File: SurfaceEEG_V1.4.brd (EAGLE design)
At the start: 160 x 100 mm, 67 parts, among them IC1 LMV602, IC2 TSZ124IQ4T, U1 MCP4442-103E/ST

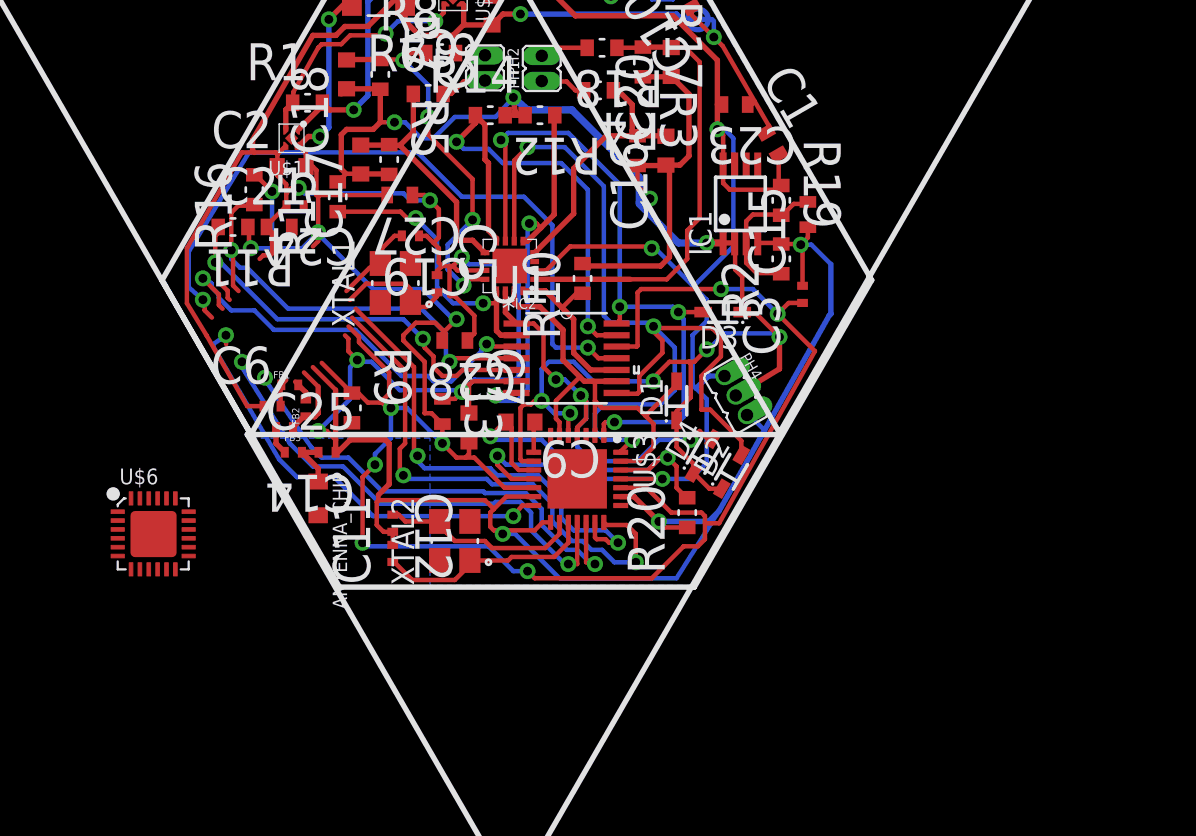
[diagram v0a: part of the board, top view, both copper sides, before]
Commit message: Started version 1.4 with atmega328
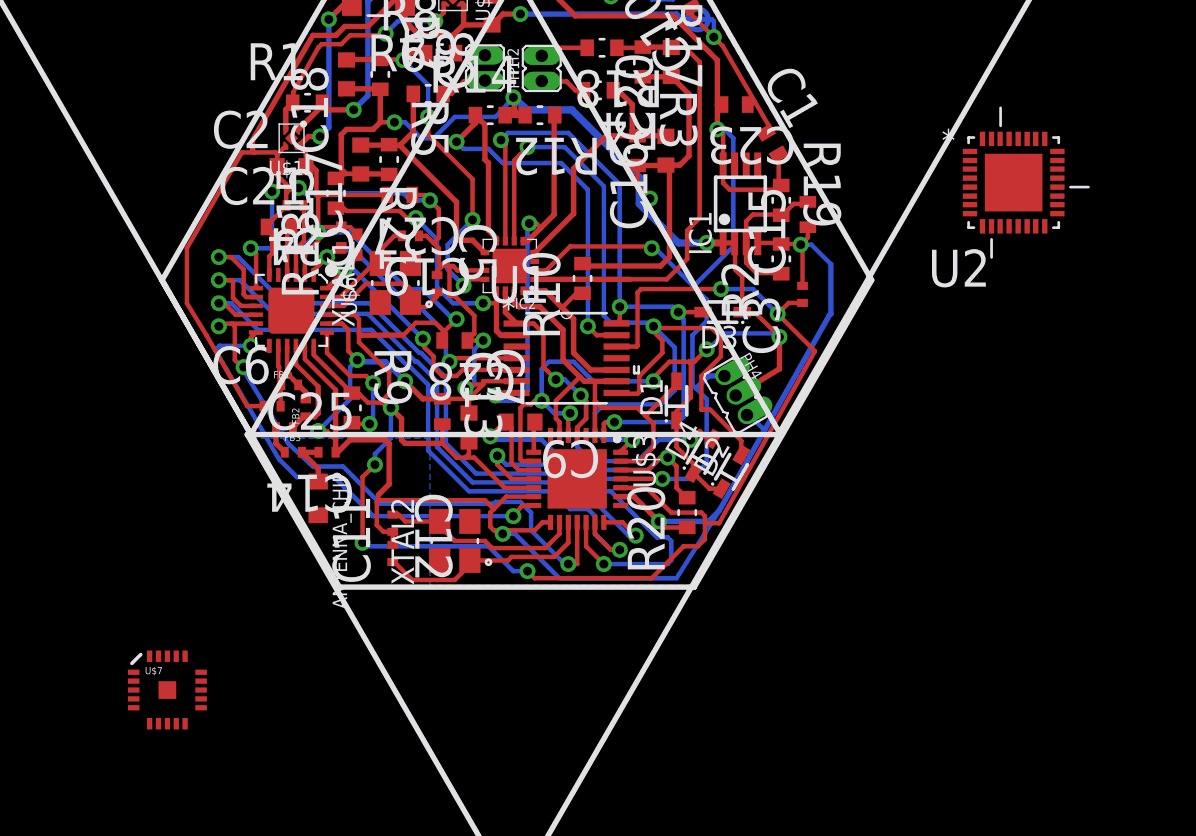
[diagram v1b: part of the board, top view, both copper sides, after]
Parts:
- removed R11, R16: 3.3K Ohms, (manufact)-resistors-YAGEO-element14:RESC1608X60N
- added R13, R21: 4.7K Ohms, (manufact)-resistors-YAGEO-element14:RESC1005X40N
- added U$7: NRF24L01SMD, (misc)-parts-that-we-use:QFN20
- added U2: ATMEGA328P-MU, (misc)-parts-that-we-use:QFN50P500X500X100-33N
- moved U$6 14.8 mm to (18.7, 32.2), turned to 270 degrees
- moved R15 0.22 mm to (21.2, 38.8)
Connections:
- new net AVCC: U2.18
- new net DVDD: U$7.19
- new net VCC_2: U2.6
- new net VSS: U$7.0, U$7.14, U$7.17, U$7.20, U$7.8
- net SCL: now also R13.1; no longer R16.1
- net SDA: now also R21.2; no longer R11.2
- net VCC: now also R13.2, R21.1, U2.4; no longer R11.1, R16.2
- net VDD: now also U$7.15, U$7.18, U$7.7
- net VDD_PA: now also U$7.11
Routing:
- net A1: track 40.3 -> 0.00 mm, vias 2 -> 0
- net A0: track 23.5 -> 0.00 mm, vias 2 -> 0
- net SCLK: track 27.0 -> 45.9 mm
- net MISO: track 26.2 -> 35.9 mm
- net SDA: track 25.0 -> 15.6 mm
- net SCL: track 26.0 -> 16.7 mm
- net N$1: track 0.00 -> 7.86 mm, vias 0 -> 2
- net MOSI: track 29.7 -> 37.0 mm
- net GND: track 207.3 -> 200.8 mm, vias 11 -> 12
- net VCC: track 139.9 -> 144.7 mm, vias 13 -> 12
- net _CS: track 27.8 -> 32.1 mm
- net N$2: track 0.02 -> 4.09 mm
- net N$3: track 0.27 -> 3.08 mm
- net ANT1: track 1.25 -> 3.71 mm
- net VDD_PA: track 1.61 -> 3.49 mm
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
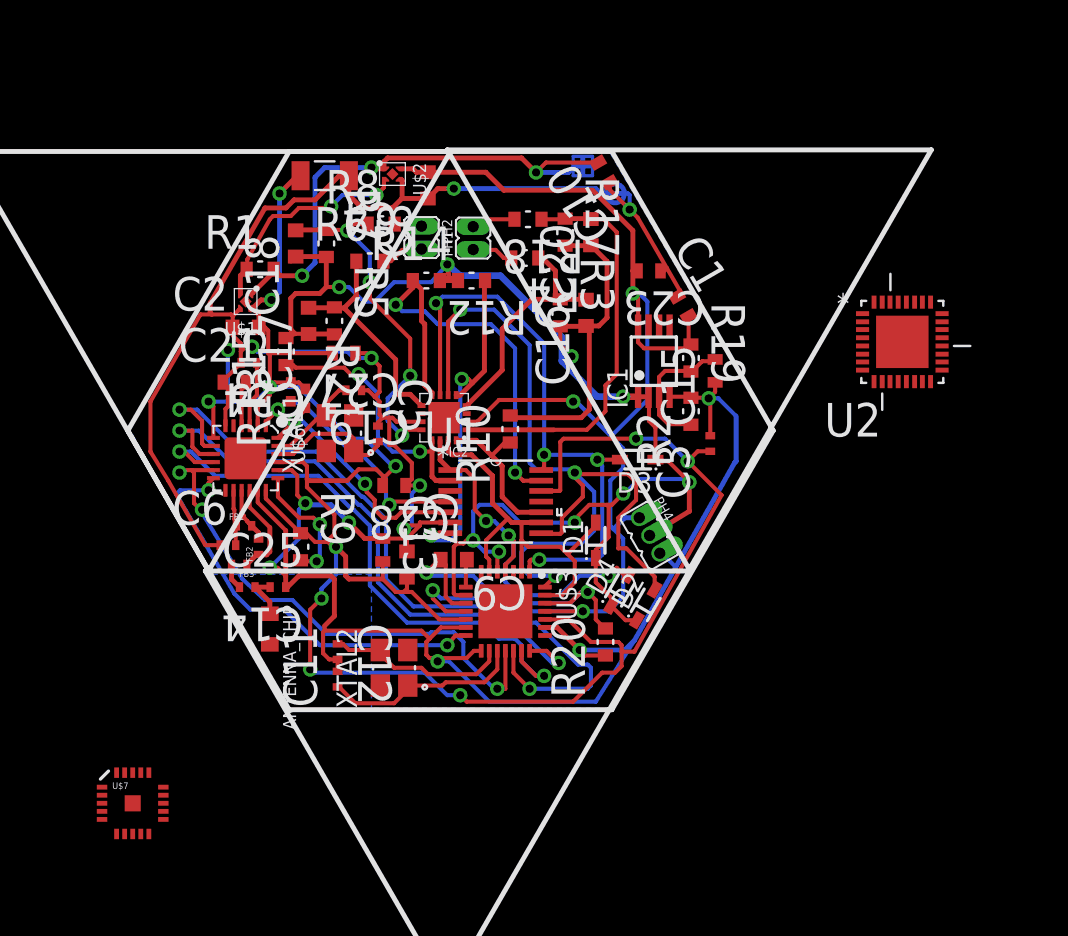
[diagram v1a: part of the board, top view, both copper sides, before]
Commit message: Version 1.4 with atmega328 and hrf24L01 ready
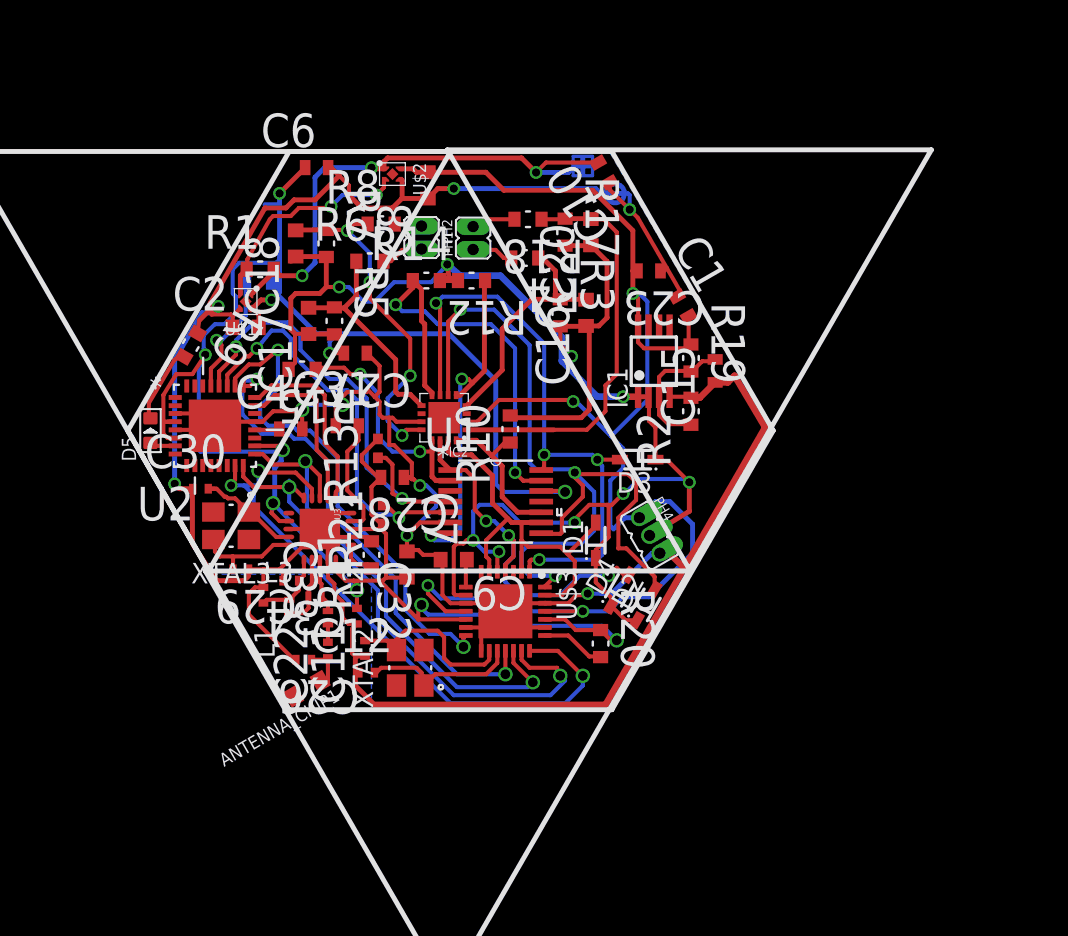
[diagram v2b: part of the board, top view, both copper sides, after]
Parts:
- removed ANTENNA_CHIP: (no value), ELL-i-Passives:R0805
- removed C13, C21: 47nF, (manufact)-Kemet-element14:CAPC1608X85N
- removed C14: 1.5pF, (manufact)-capacitors-AVX-element14:CAPC1005X60N
- removed C19, C5: 15pF, (manufact)-capacitors-AVX-element14:CAPC1005X60N
- removed C24, C3: 0.1uF, (manufact)-capacitors-AVX-element14:CAPC1005X60N
- removed C25: 1pF, (manufact)-capacitors-AVX-element14:CAPC1005X60N
- removed FB1, FB2: 6.8nH, ELL-i-Passives:FB0402
- removed FB3: 4.7nH, ELL-i-Passives:FB0402
- removed U$6: NRF24LE1-24, (misc)-parts-that-we-use:QFN24G-0.5-4X4MM
- removed U$7: NRF24L01SMD, (misc)-parts-that-we-use:QFN20
- removed XTAL1: 7M-16.000MAAJ-T, (misc)-parts-that-we-use:TXC_7M-16.000MAAJ-T
- added ANTENNA_CHIP1: (no value), ELL-i-Passives:R0805
- added C22: 1.5pF, (manufact)-capacitors-AVX-element14:CAPC1005X60N
- added C26: 1pF, (manufact)-capacitors-AVX-element14:CAPC1005X60N
- added C29, C30: 15pF, (manufact)-capacitors-AVX-element14:CAPC1005X60N
- added C31: 47nF, (manufact)-Kemet-element14:CAPC1608X85N
- added C32: 0.1uF, (manufact)-capacitors-AVX-element14:CAPC1005X60N
- added C33: 2.2nF, (manufact)-Kemet-element14:CAPC1005X60N
- added C34: 4.7pF, (manufact)-capacitors-AVX-element14:CAPC1005X60N
- added D5: BLUE-0603, Seeed-OPL-Diode:LED-0603
- added L1: 2.7nH, (manufact)-inductors-WE-KI-element14:WE-KI_0402A
- added L2: 3.9nH, (manufact)-inductors-WE-KI-element14:WE-KI_0402A
- added L3: 8.2nH, (manufact)-inductors-WE-KI-element14:WE-KI_0402A
- added R11: 22K Ohms, (manufact)-resistors-YAGEO-element14:RESC1608X60N
- added R16: 10K Ohm, (manufact)-resistors-YAGEO-element14:RESC1608X60N
- added U3: NRF24L01ALT1, Testing:QFN20_ALT1
- added XTAL3: 7M-16.000MAAJ-T, (misc)-parts-that-we-use:TXC_7M-16.000MAAJ-T
- C4: value 100UF -> 100nF; device (manufact)-capacitors-AVX-element14:CAPC3216X178N -> (manufact)-Kemet-element14:CAPC1608X85N
- C6: value 2.2nF -> 10nF; device (manufact)-Kemet-element14:CAPC1005X60N -> (manufact)-Kemet-element14:CAPC1608X85N
- R20: value 0 Ohm -> 88.7K EDIT
- R9: value 22K Ohms -> 3.3K Ohms
- moved U2 42.9 mm to (16.8, 34.2)
- moved C6 24.0 mm to (23.1, 50.2)
- moved C4 15.8 mm to (21.5, 34.0), turned to 0 degrees
- moved R9 14.2 mm to (15.3, 39.2), turned to 240 degrees
- moved R21 8.65 mm to (27.2, 28.7), turned to 90 degrees
- moved R13 6.44 mm to (26.9, 32.8)
- moved C12 1.84 mm to (26.2, 18.9), turned to 0 degrees
- moved C11 1.71 mm to (26.1, 20.4)
- moved R15 1.49 mm to (22.2, 37.7), turned to 180 degrees
- moved XTAL2 1.00 mm to (28.9, 19.2)
- moved C27 0.70 mm to (25.5, 38.7)
- moved C28 0.51 mm to (27.8, 31.0)
- moved R20 0.32 mm to (40.7, 20.7), turned to 270 degrees
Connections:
- removed net AGND: C9.2, R20.2, U$3.10, U$3.26
- removed net AVCC: U2.18
- removed net DVDD: U$7.19
- removed net N$10: C5.2, U$6.22, XTAL1.1
- removed net N$11: C19.2, U$6.23, XTAL1.3
- removed net N$22: C14.2, FB3.2
- removed net N$3: C21.2, U$6.4
- removed net VCC_2: U2.6
- removed net VDD_PA: C6.2, FB1.1, U$6.14, U$7.11
- removed net VSS: U$7.0, U$7.14, U$7.17, U$7.20, U$7.8
- removed net _CS: U$3.18, U$6.11
- new net CE: U2.24, U3.1
- new net MCP_CS: U$3.18, U2.25
- new net N$13: C22.2, L2.2
- new net N$16: C33.2, C34.1, L1.2, U3.11
- new net N$19: R11.1, U3.16
- new net N$20: C31.2, U3.19
- new net N$7: C4.1, U2.20
- new net N$8: C30.2, U3.9, XTAL3.1
- new net N$9: C29.2, U3.10, XTAL3.3
- new net NRF_CS: U2.23, U3.2
- new net RESET: R16.1, U2.29
- net ANT: now also ANTENNA_CHIP1.1, C22.1, C26.1; no longer ANTENNA_CHIP.1, C14.1, C25.1
- net ANT1: now also L1.1, L3.1, U3.12; no longer FB1.2, FB2.2, U$6.15
- net ANT2: now also L2.1, L3.2, U3.13; no longer FB2.1, FB3.1, U$6.16
- net GND: now also C26.2, C29.1, C30.1, C31.1, C32.2, C33.1, C34.2, C4.2, C6.2, C9.2, R11.2, R9.1, U$3.10, U$3.26, U2.21, U2.3, U2.33, U2.5, U3.0, U3.14, U3.17, U3.20, U3.8; no longer C13.1, C19.1, C21.1, C24.2, C25.2, C3.2, C4.1, C5.1, C6.1, R20.1, U$6.17, U$6.20, U$6.6
- net MISO: now also U2.16, U3.5; no longer U$6.10
- net MOSI: now also U2.15, U3.4; no longer U$6.9
- net N$1: now also D5.+, U2.7; no longer R9.2, U$6.19
- net N$2: now also D5.-, R9.2; no longer C24.1, U$6.3
- net SCL: now also U2.28; no longer U$6.1
- net SCLK: now also U2.17, U3.3; no longer U$6.8
- net SDA: now also U2.27; no longer U$6.24
- net VCC: now also C32.1, C6.1, R16.2, R20.1, U2.18, U2.6, U3.15, U3.18, U3.7; no longer C13.2, C3.1, C4.2, R9.1, U$6.18, U$6.2, U$6.21, U$6.7
- net VDD: no longer U$7.15, U$7.18, U$7.7
- net _DR: now also U2.26; no longer U$6.12
- net _RESET: now also R20.2
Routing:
- net _CS: track 32.1 -> 0.00 mm, vias 2 -> 0
- net MCP_CS: track 0.00 -> 31.5 mm, vias 0 -> 2
- net AGND: track 22.8 -> 0.00 mm, vias 2 -> 0
- net GND: track 200.8 -> 222.7 mm, vias 12 -> 9
- net SCLK: track 45.9 -> 31.3 mm
- net CE: track 0.00 -> 11.6 mm
- net SCL: track 16.7 -> 28.1 mm
- net NRF_CS: track 0.00 -> 10.6 mm
- net SDA: track 15.6 -> 26.0 mm
- net VCC: track 144.7 -> 134.4 mm, vias 12 -> 10
- net N$10: track 8.18 -> 0.00 mm
- net VDD: track 80.2 -> 88.1 mm
- net RESET: track 0.00 -> 7.77 mm, vias 0 -> 1
- net N$20: track 0.00 -> 7.33 mm
- net N$8: track 0.00 -> 6.65 mm
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
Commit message: Updated all boards in order to comply with DRC
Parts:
- PH4: value PH1X3 -> PH1X3-05LONG; device (misc)-parts-that-we-use:PH005-1-3 -> (misc)-parts-that-we-use:PHL005-1-3
- moved C6 17.7 mm to (12.8, 35.8)
- moved PH4 17.7 mm to (32.8, 14.1)
- moved R12 17.7 mm to (22.4, 28.8)
- moved R3 17.7 mm to (27.9, 26.8)
- moved R8 17.7 mm to (16.8, 32.3)
- moved U1 17.7 mm to (23.9, 15.1)
- moved C17 17.7 mm to (12.3, 26.3)
- moved C20 17.7 mm to (29.8, 31.8)
- moved C22 17.7 mm to (13.5, 5.90)
- moved C23 17.7 mm to (33.4, 29.4)
- moved C27 17.7 mm to (15.2, 24.3)
- moved C29 17.7 mm to (8.10, 10.9)
- moved C30 17.7 mm to (5.60, 15.9)
- moved C31 17.7 mm to (14.7, 19.8)
- moved C34 17.7 mm to (11.2, 10.2)
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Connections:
- net GND: now also PH4.3; no longer PH4.P$3
- net GNDI: now also PH4.2; no longer PH4.P$2
- net VDD: now also PH4.1; no longer PH4.P$1
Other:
- board size 160 x 100 mm -> 41.2 x 35.5 mm

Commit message: added led
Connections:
- new net N$10: U2.10
- new net N$3: U2.1
- new net N$6: U2.9
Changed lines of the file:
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@@
 <layer number="23" name="tOrigins" color="15" fill="1" visible="yes" active="yes"/>
 <layer number="24" name="bOrigins" color="15" fill="1" visible="yes" active="yes"/>
-<layer number="25" name="tNames" color="7" fill="1" visible="yes" active="yes"/>
-<layer number="26" name="bNames" color="7" fill="1" visible="yes" active="yes"/>
-<layer number="27" name="tValues" color="7" fill="1" visible="yes" active="yes"/>
-<layer number="28" name="bValues" color="7" fill="1" visible="yes" active="yes"/>
+<layer number="25" name="tNames" color="7" fill="1" visible="no" active="yes"/>
+<layer number="26" name="bNames" color="7" fill="1" visible="no" active="yes"/>
+<layer number="27" name="tValues" color="7" fill="1" visible="no" active="yes"/>
+<layer number="28" name="bValues" color="7" fill="1" visible="no" active="yes"/>
 <layer number="29" name="tStop" color="7" fill="3" visible="yes" active="yes"/>
 <layer number="30" name="bStop" color="7" fill="6" visible="yes" active="yes"/>
@@
 <wire x1="4.3" y1="15.9" x2="4" y2="16.2" width="0.3048" layer="1"/>
 <via x="4" y="16.2" extent="1-16" drill="0.5" shape="octagon"/>
-<wire x1="4" y1="16.2" x2="4" y2="23.9" width="0.3048" layer="16"/>
 <wire x1="4" y1="23.9" x2="5.7" y2="26.8" width="0.3048" layer="16"/>
 <wire x1="5.7" y1="26.8" x2="6.3" y2="26.8" width="0.3048" layer="16"/>
@@
 <wire x1="6.35" y1="26.85" x2="6.7" y2="27.2" width="0.3048" layer="1"/>
 <wire x1="7.6" y1="25.8872" x2="7.6" y2="25.7" width="0.3048" layer="1"/>
+<wire x1="4" y1="16.2" x2="4" y2="23.9" width="0.3048" layer="16"/>
 </signal>
 <signal name="VCC">
@@
 <wire x1="4.0362" y1="20.054" x2="3.354" y2="20.054" width="0.254" layer="1"/>
 <wire x1="3.354" y1="20.054" x2="3.3" y2="20" width="0.254" layer="1"/>
-<wire x1="3.3" y1="21.7" x2="4.1" y2="23" width="0.254" layer="1"/>
 <wire x1="4.1" y1="23" x2="5.1" y2="23" width="0.254" layer="1"/>
 <wire x1="14.9254" y1="13.4" x2="16.8" y2="13.4" width="0.254" layer="1"/>
@@
 <wire x1="5.6" y1="18.2" x2="5.5" y2="18.3" width="0.254" layer="16"/>
 <wire x1="5.5" y1="18.3" x2="5.5" y2="23.4" width="0.254" layer="16"/>
-<wire x1="5.6" y1="18.2" x2="10.6" y2="18.2" width="0.254" layer="16"/>
 <wire x1="10.6" y1="18.2" x2="10.7" y2="18.3" width="0.254" layer="16"/>
 <wire x1="10.4446" y1="18.5554" x2="10.7" y2="18.3" width="0.254" layer="1"/>
@@
 <wire x1="13.6" y1="24.3" x2="13.6" y2="25" width="0.254" layer="16"/>
 <wire x1="13.6" y1="25" x2="14.1" y2="25.5" width="0.254" layer="16"/>
+<wire x1="3.3" y1="21.7" x2="4.1" y2="23" width="0.254" layer="1"/>
+<wire x1="5.6" y1="18.2" x2="10.6" y2="18.2" width="0.254" layer="16"/>
 </signal>
 <signal name="MOSI">
@@
 <wire x1="26" y1="24.8" x2="23.8" y2="27" width="0.254" layer="16"/>
 <wire x1="23.8" y1="27" x2="21.7" y2="27" width="0.254" layer="16"/>
-<wire x1="20.95" y1="21.7" x2="20.95" y2="26.25" width="0.254" layer="1"/>
 <wire x1="20.95" y1="26.25" x2="21.7" y2="27" width="0.254" layer="1"/>
 <wire x1="28.8" y1="16.9" x2="30" y2="15.7" width="0.254" layer="16"/>
@@
 <wire x1="33.75" y1="9.652625" x2="33.75" y2="10.45" width="0.254" layer="1"/>
 <wire x1="33.75" y1="10.45" x2="32" y2="12.2" width="0.254" layer="1"/>
+<wire x1="20.95" y1="21.7" x2="20.95" y2="26.25" width="0.254" layer="1"/>
 </signal>
 <signal name="CH2_F_A">
@@
 <contactref element="U1" pad="14"/>
 <contactref element="U$3" pad="1"/>
-<wire x1="20.45" y1="21.7" x2="20.45" y2="27.15" width="0.254" layer="1"/>
 <via x="20.2" y="27.4" extent="1-16" drill="0.5" diameter="0.6096" shape="octagon"/>
 <wire x1="26.9" y1="24.9" x2="26.9" y2="18" width="0.254" layer="16"/>
@@
 <wire x1="26.9" y1="18" x2="29.9" y2="18" width="0.254" layer="16"/>
 <wire x1="29.9" y1="18" x2="30.2" y2="17.7" width="0.254" layer="16"/>
+<wire x1="20.45" y1="21.7" x2="20.45" y2="27.15" width="0.254" layer="1"/>
 </signal>
 <signal name="CH3_F_A">
@@
 <wire x1="2.4" y1="20.362" x2="2.5" y2="20.262" width="0.254" layer="1"/>
 </signal>
+<signal name="N$3">
+<contactref element="U2" pad="1"/>
+</signal>
+<signal name="N$6">
+<contactref element="U2" pad="9"/>
+</signal>
+<signal name="N$10">
+<contactref element="U2" pad="10"/>
+</signal>
 </signals>
